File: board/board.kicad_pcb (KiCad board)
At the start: 2 copper layers, 113 parts, among them J202 Conn_01x02, J301 Conn_Coaxial, J401 Conn_Coaxial, Q201 CPH3350, U101 Pico, U102 CS42438, U201 AZ1117-ADJ, U202 L7805, U203 L7805, U301 lmc6042, U401 lmc6042

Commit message: some layout
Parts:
- removed TP101, TP102, TP103, TP104, TP105, TP106, TP107, TP108, TP109: x, TestPoint:TestPoint_Pad_D2.5mm
- J401, NT201, NT202, NT203: moved to B.Cu
- moved H101 173.6 mm to (271.5, 19.8)
- moved H102 158.7 mm to (275.9, 30.8)
- moved H103 158.7 mm to (269.5, 45.1)
- moved H104 158.7 mm to (277.4, 38.7)
- moved U201 89.1 mm to (220.7, 119.7), turned to 90 degrees
- moved NT202 86.1 mm to (225.6, 125.4), turned to 90 degrees
- moved C206 83.6 mm to (222.2, 127.3), turned to 180 degrees
- moved FB203 83.3 mm to (222.5, 129.4)
- moved R110 79.2 mm to (190.4, 82.7), turned to -90 degrees
- moved U203 79.2 mm to (197.5, 127.2), turned to 90 degrees
- moved C109 78.2 mm to (180.7, 81.5), turned to -90 degrees
- moved C212 77.4 mm to (225.4, 120.2), turned to 90 degrees
- moved C209 76.5 mm to (225.4, 116.2), turned to -90 degrees
- moved C111 76.2 mm to (150.5, 133.7), turned to -90 degrees
- moved C112 76.2 mm to (178.7, 81.5), turned to -90 degrees
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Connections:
- R107 pad 2: GNDA -> GNDD
- R301 pad 1: /out_1_p -> /out_2_P
- R302 pad 1: /out_1_n -> /out_2_N
- R401 pad 1: /out_2_p -> /out_1_N
- R402 pad 1: /out_2_n -> /out_1_P
- U102 pad 19: /out_1_n -> /out_1_N
- U102 pad 20: /out_1_p -> /out_1_P
- U102 pad 21: /out_2_p -> /out_2_P
- U102 pad 22: /out_2_n -> /out_2_N
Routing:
- net GNDA: track 0.00 -> 97.7 mm, vias 0 -> 12
- net /out_1_N: track 0.00 -> 46.1 mm
- net /out_1_P: track 0.00 -> 45.6 mm
- net VDDA: track 0.00 -> 23.1 mm
- net /dac_mclk_term: track 0.00 -> 19.2 mm
- net /dac_sclk_term: track 0.00 -> 17.9 mm
- net /dac_sdout: track 0.00 -> 17.4 mm
- net +5VD: track 0.00 -> 16.0 mm
- net GNDPWR: track 0.00 -> 15.8 mm, vias 0 -> 3
- net GNDD: track 0.00 -> 14.1 mm, vias 0 -> 5
- net /dac_fs_term: track 0.00 -> 13.3 mm
- net /out_2_N: track 0.00 -> 13.2 mm
- net /output_stage/dac_filt_out: track 0.00 -> 13.0 mm
- net /out_2_P: track 0.00 -> 12.7 mm
- net /output_stage1/dac_filt_out: track 0.00 -> 12.4 mm
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
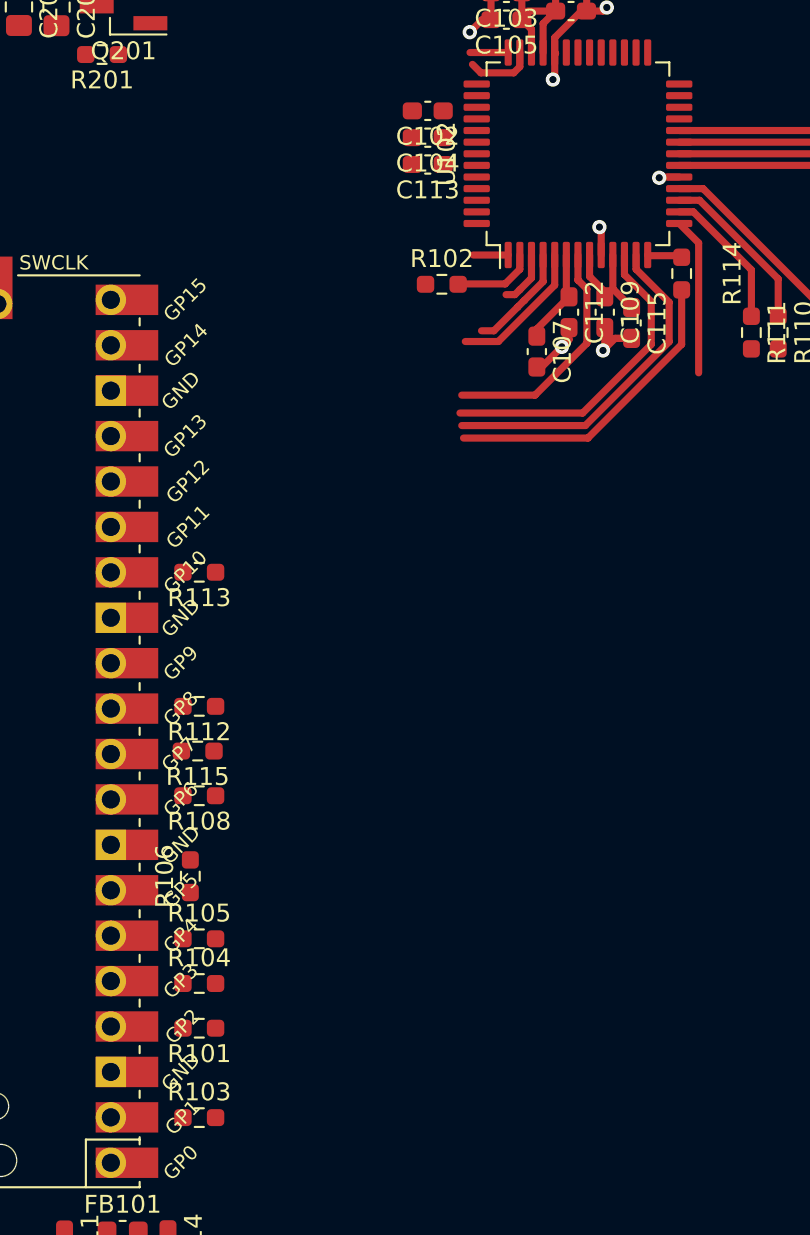
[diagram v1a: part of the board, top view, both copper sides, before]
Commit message: Some more layout, digital side has been reorganized
looking into single to diff conversion. with the biases
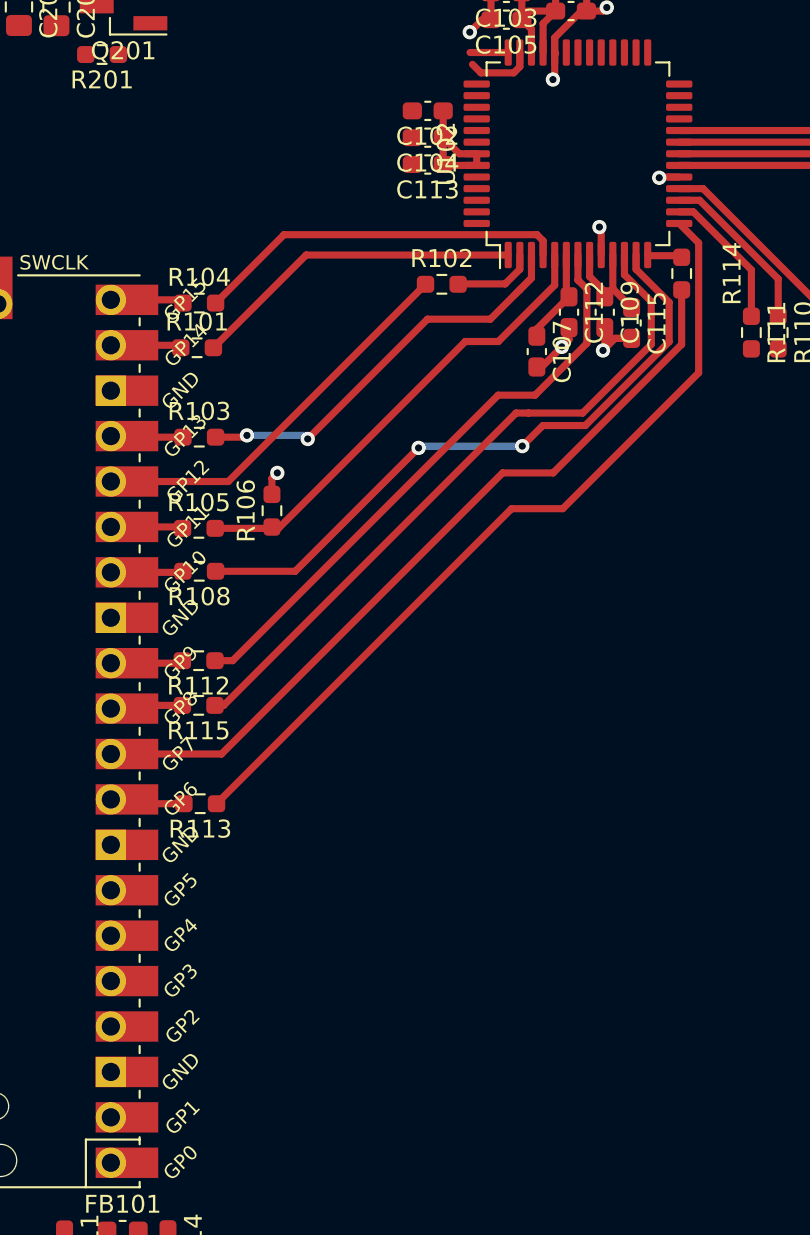
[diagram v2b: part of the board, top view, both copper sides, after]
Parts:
- moved R101 38.1 mm to (157.9, 83.5), turned to 0 degrees
- moved R103 38.1 mm to (158.0, 88.5)
- moved R104 38.1 mm to (158.0, 81.0)
- moved R105 23.0 mm to (158.0, 93.6)
- moved R106 20.9 mm to (162.1, 92.6)
- moved R113 12.9 mm to (158.1, 109.0)
- moved R108 12.6 mm to (158.0, 96.0)
- moved R115 2.56 mm to (158.0, 103.5)
- moved R112 2.56 mm to (158.0, 101.0)
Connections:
- U101 pad 1: /dac_ctrl_cipo -> unconnected-(U101-Pad1)
- U101 pad 10: /dac_sclk -> /dac_sdout
- U101 pad 11: /dac_fs -> /dac_sclk
- U101 pad 12: /dac_sdout -> /dac_fs
- U101 pad 14: /dac_sdin -> /dac_mclk
- U101 pad 15: unconnected-(U101-Pad15) -> /dac_ctrl_rstn
- U101 pad 16: unconnected-(U101-Pad16) -> /dac_ctrl_cipo
- U101 pad 17: unconnected-(U101-Pad17) -> /dac_ctrl_csn
- U101 pad 19: unconnected-(U101-Pad19) -> /dac_ctrl_clk
- U101 pad 2: /dac_ctrl_csn -> unconnected-(U101-Pad2)
- U101 pad 20: unconnected-(U101-Pad20) -> /dac_ctrl_copi
- U101 pad 4: /dac_ctrl_clk -> unconnected-(U101-Pad4)
- U101 pad 5: /dac_ctrl_copi -> unconnected-(U101-Pad5)
- U101 pad 6: /dac_ctrl_rstn -> unconnected-(U101-Pad6)
- U101 pad 9: /dac_mclk -> /dac_sdin
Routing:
- net /dac_sdin_term: track 8.80 -> 45.7 mm
- net /dac_sdout: track 17.4 -> 44.5 mm
- net /dac_ctrl_cipo: track 0.00 -> 22.2 mm
- net /dac_ctrl_csn_term: track 3.10 -> 24.1 mm, vias 0 -> 2
- net /dac_sclk_term: track 17.9 -> 38.4 mm
- net /dac_fs_term: track 13.3 -> 33.3 mm
- net /dac_ctrl_rstn_term: track 7.99 -> 26.3 mm
- net /dac_mclk_term: track 19.2 -> 36.3 mm, vias 0 -> 2
- net /dac_ctrl_clk_term: track 1.96 -> 18.6 mm
- net /dac_ctrl_copi_term: track 6.07 -> 20.8 mm
- net +5VD: track 16.0 -> 23.8 mm
- net /dac_sdin: track 0.00 -> 4.18 mm
- net /dac_ctrl_copi: track 0.00 -> 4.11 mm
- net /dac_sclk: track 0.00 -> 4.07 mm
- net /dac_mclk: track 0.00 -> 4.06 mm
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
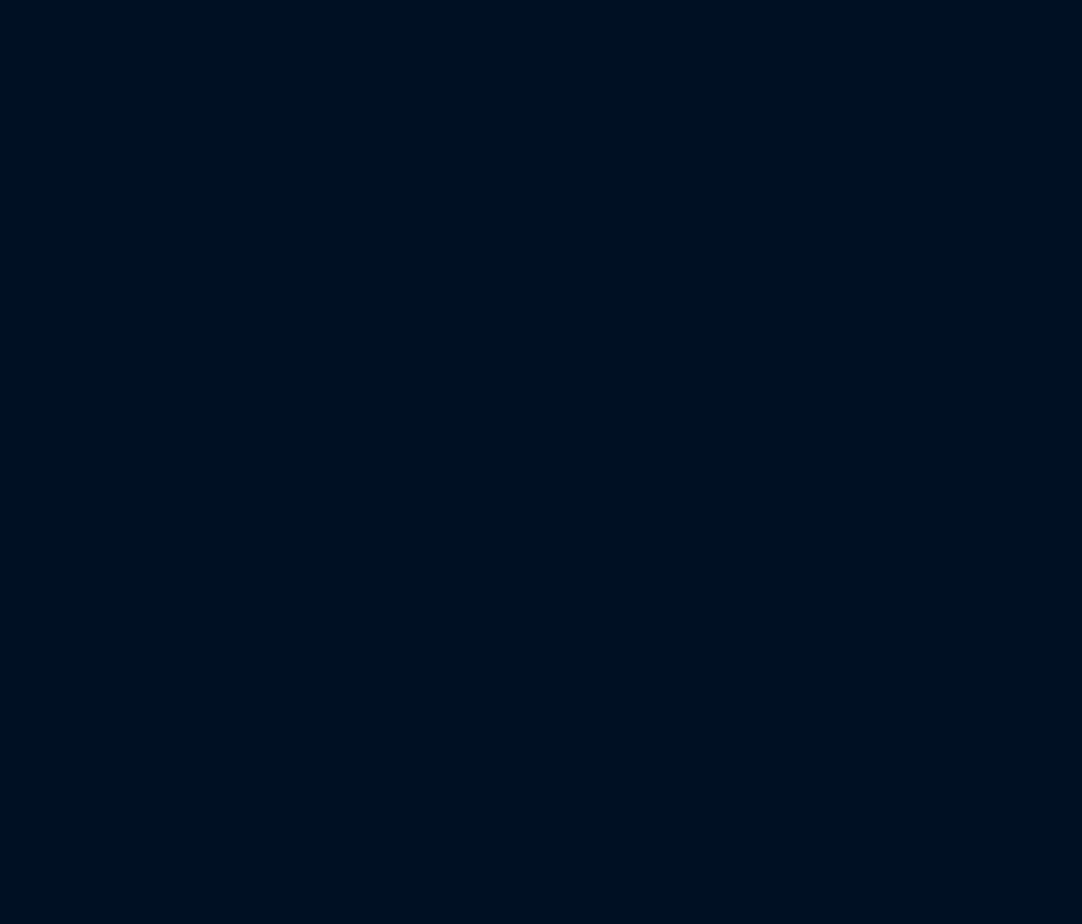
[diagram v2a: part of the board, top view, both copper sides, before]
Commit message: Finalize input tranz amp, to diff, protection
layout left
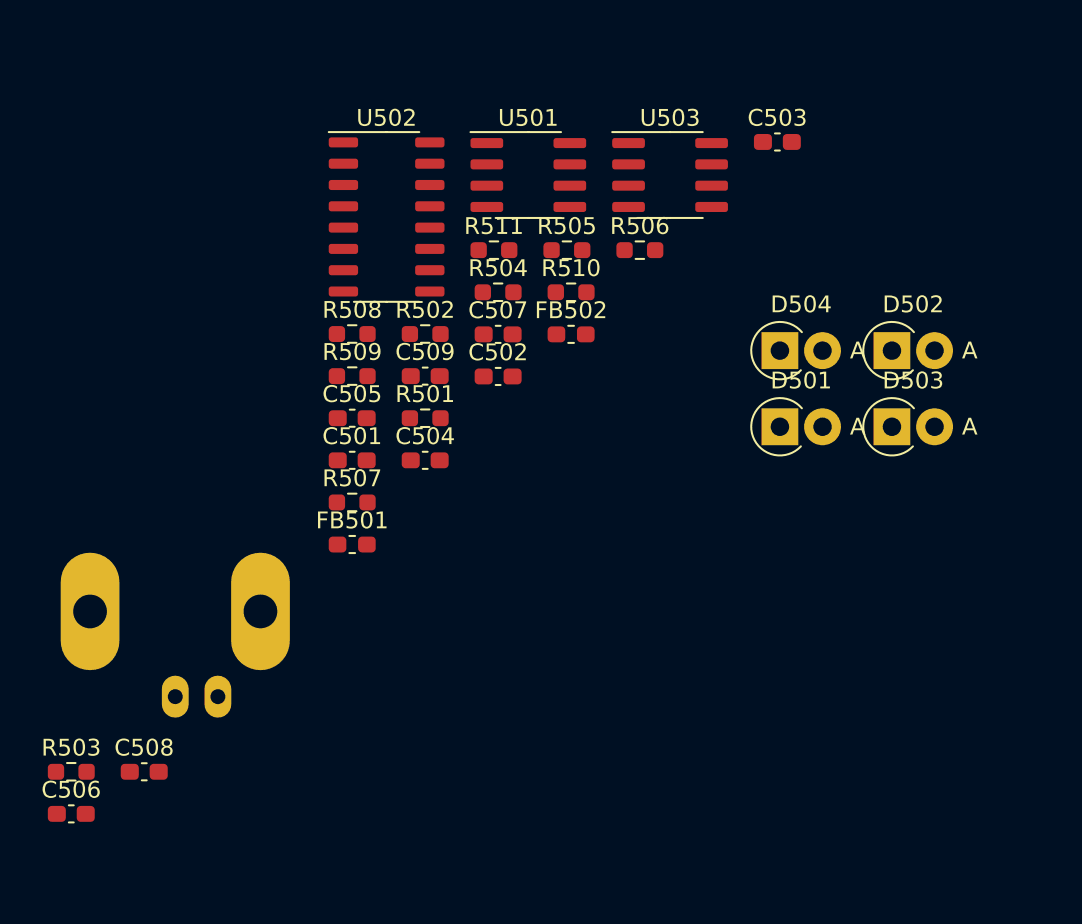
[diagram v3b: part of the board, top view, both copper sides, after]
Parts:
- added C501: 22u, Capacitor_SMD:C_0603_1608Metric_Pad1.08x0.95mm_HandSolder, F.Cu at (75.8, 47.8)
- added C502: 10p, Capacitor_SMD:C_0603_1608Metric_Pad1.08x0.95mm_HandSolder, F.Cu at (84.5, 42.8)
- added C503: 100n, Capacitor_SMD:C_0603_1608Metric_Pad1.08x0.95mm_HandSolder, F.Cu at (101.1, 28.8)
- added C504: 100n, Capacitor_SMD:C_0603_1608Metric_Pad1.08x0.95mm_HandSolder, F.Cu at (80.1, 47.8)
- added C505: 22u, Capacitor_SMD:C_0603_1608Metric_Pad1.08x0.95mm_HandSolder, F.Cu at (75.8, 45.2)
- added C506: 100n, Capacitor_SMD:C_0603_1608Metric_Pad1.08x0.95mm_HandSolder, F.Cu at (59.0, 68.8)
- added C507: 10p, Capacitor_SMD:C_0603_1608Metric_Pad1.08x0.95mm_HandSolder, F.Cu at (84.5, 40.2)
- added C508: 100n, Capacitor_SMD:C_0603_1608Metric_Pad1.08x0.95mm_HandSolder, F.Cu at (63.4, 66.3)
- added C509: 100n, Capacitor_SMD:C_0603_1608Metric_Pad1.08x0.95mm_HandSolder, F.Cu at (80.1, 42.7)
- added D501: 3v9, Diode_THT:D_DO-41_SOD81_P2.54mm_Vertical_AnodeUp, F.Cu at (101.2, 45.8)
- added D502: 3v9, Diode_THT:D_DO-41_SOD81_P2.54mm_Vertical_AnodeUp, F.Cu at (107.9, 41.2)
- added D503: 3v9, Diode_THT:D_DO-41_SOD81_P2.54mm_Vertical_AnodeUp, F.Cu at (107.9, 45.8)
- added D504: 3v9, Diode_THT:D_DO-41_SOD81_P2.54mm_Vertical_AnodeUp, F.Cu at (101.2, 41.2)
- added FB501: BLM18AG102SN1D, Inductor_SMD:L_0603_1608Metric_Pad1.05x0.95mm_HandSolder, F.Cu at (75.8, 52.8)
- added FB502: BLM18AG102SN1D, Inductor_SMD:L_0603_1608Metric_Pad1.05x0.95mm_HandSolder, F.Cu at (88.8, 40.2)
- added J501: Conn_Coaxial, Connector_Coaxial:BNC_Amphenol_B6252HB-NPP3G-50_Horizontal, B.Cu at (65.2, 61.8)
- added R501: 1M, Resistor_SMD:R_0603_1608Metric_Pad0.98x0.95mm_HandSolder, F.Cu at (80.1, 45.2)
- added R502: 100k, Resistor_SMD:R_0603_1608Metric_Pad0.98x0.95mm_HandSolder, F.Cu at (80.1, 40.2)
- added R503: 10k, Resistor_SMD:R_0603_1608Metric_Pad0.98x0.95mm_HandSolder, F.Cu at (59.0, 66.3)
- added R504: 1k, Resistor_SMD:R_0603_1608Metric_Pad0.98x0.95mm_HandSolder, F.Cu at (84.5, 37.7)
- added R505: 10k, Resistor_SMD:R_0603_1608Metric_Pad0.98x0.95mm_HandSolder, F.Cu at (88.5, 35.2)
- added R506: 10k, Resistor_SMD:R_0603_1608Metric_Pad0.98x0.95mm_HandSolder, F.Cu at (92.9, 35.2)
- added R507: 10k, Resistor_SMD:R_0603_1608Metric_Pad0.98x0.95mm_HandSolder, F.Cu at (75.8, 50.3)
- added R508: 10k, Resistor_SMD:R_0603_1608Metric_Pad0.98x0.95mm_HandSolder, F.Cu at (75.8, 40.2)
- added R509: 10k, Resistor_SMD:R_0603_1608Metric_Pad0.98x0.95mm_HandSolder, F.Cu at (75.8, 42.7)
- added R510: 33, Resistor_SMD:R_0603_1608Metric_Pad0.98x0.95mm_HandSolder, F.Cu at (88.8, 37.7)
- added R511: 33, Resistor_SMD:R_0603_1608Metric_Pad0.98x0.95mm_HandSolder, F.Cu at (84.2, 35.2)
- added U501: lmc6042, Package_SO:SOIC-8_3.9x4.9mm_P1.27mm, F.Cu at (86.2, 30.7)
- added U502: HEF4053B, Package_SO:SO-16_3.9x9.9mm_P1.27mm, F.Cu at (77.8, 33.2)
- added U503: lmc6042, Package_SO:SOIC-8_3.9x4.9mm_P1.27mm, F.Cu at (94.7, 30.7)
